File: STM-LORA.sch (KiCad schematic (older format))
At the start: 22 parts, among them J1 Batt, J10 CONN_02X07, J11 CONN_02X09, J12 CONN_01X02, J13 CONN_01X02, J14 CONN_01X02, J15 CONN_01X03, J2 Solar, J3 CONN_01X17, J4 CONN_01X03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

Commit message: edit front plane and readd fp-lib-table
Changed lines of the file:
@@
 LIBS:stm32f103c8t6-module-china
 LIBS:RFM95
+LIBS:STM-LORA-cache
 EELAYER 25 0
 EELAYER END
@@
 $EndComp
 Wire Wire Line
-	7750 1900 8800 1900
-Wire Wire Line
-	8800 1900 9100 1900
+	7750 1900 9100 1900
 Wire Wire Line
 	3900 3600 4700 3600
@@
 	6000 3400 6000 6500
 Wire Wire Line
-	6000 6500 1100 6500
-Wire Wire Line
-	1100 6500 1100 4050
-Wire Wire Line
-	1100 4050 1100 2050
+	1100 6500 6000 6500
+Wire Wire Line
+	1100 2050 1100 6500
 Wire Wire Line
 	1100 4050 1800 4050
@@
 	8800 1900 8800 2250
 Wire Wire Line
-	8800 2850 9000 2850
-Wire Wire Line
-	9000 2850 9100 2850
+	8800 2850 9100 2850
 Wire Wire Line
 	7550 4500 8850 4500
@@
 	1700 4950 1800 4950
 Wire Wire Line
-	3900 2550 4400 2550
-Wire Wire Line
-	4400 2550 4800 2550
-Wire Wire Line
-	4800 2550 5250 2550
+	3900 2550 5250 2550
 Wire Wire Line
 	5250 2550 5250 2950
@@
 	5750 2150 6200 2150
 Wire Wire Line
-	2950 6950 2950 7050
-Wire Wire Line
-	2950 7050 2950 7150
-Wire Wire Line
-	2950 7150 2950 7250
-Wire Wire Line
-	2950 7250 2950 7350
+	2950 6950 2950 7350
 Connection ~ 2950 7050
 Connection ~ 2950 7150
@@
 $EndComp
 Wire Wire Line
-	3500 6950 3500 7050
-Wire Wire Line
-	3500 7050 3500 7150
-Wire Wire Line
-	3500 7150 3500 7250
-Wire Wire Line
-	3500 7250 3500 7350
+	3500 6950 3500 7350
 Connection ~ 3500 7050
 Connection ~ 3500 7150

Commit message: Start bigger NG board
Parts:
- added J16: CONN_01X01, Pin_Headers:Pin_Header_Straight_1x01_Pitch2.54mm, symbol CONN_01X01
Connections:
- net at U2.9 (ANA): now also J16.1 (P1)
- no-connect marks 48 -> 47
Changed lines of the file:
@@
 Sheet 1 1
 Title "STM32 RFM95 Proto Board"
-Date "2017-04-01"
-Rev "0.2"
+Date "2017-06-10"
+Rev "0.3"
 Comp "http://v7f.eu"
 Comment1 ""
@@
 $EndComp
 NoConn ~ 3900 4800
-NoConn ~ 4700 3150
 NoConn ~ 5800 3500
 NoConn ~ 5800 3600
@@
 	6000 3400 6000 6500
 Wire Wire Line
-	1100 6500 6000 6500
-Wire Wire Line
-	1100 2050 1100 6500
+	6000 6500 1100 6500
+Wire Wire Line
+	1100 6500 1100 2050
 Wire Wire Line
 	1100 4050 1800 4050
@@
 NoConn ~ 9400 5650
 NoConn ~ 9400 5750
+$Comp
+L CONN_01X01 J16
+U 1 1 593BCF25
+P 4700 2950
+F 0 "J16" H 4700 3050 50  0000 C CNN
+F 1 "CONN_01X01" V 4800 2950 50  0000 C CNN
+F 2 "Pin_Headers:Pin_Header_Straight_1x01_Pitch2.54mm" H 4700 2950 50  0001 C CNN
+F 3 "" H 4700 2950 50  0001 C CNN
+	1    4700 2950
+	0    -1   -1   0
+$EndComp
 $EndSCHEMATC

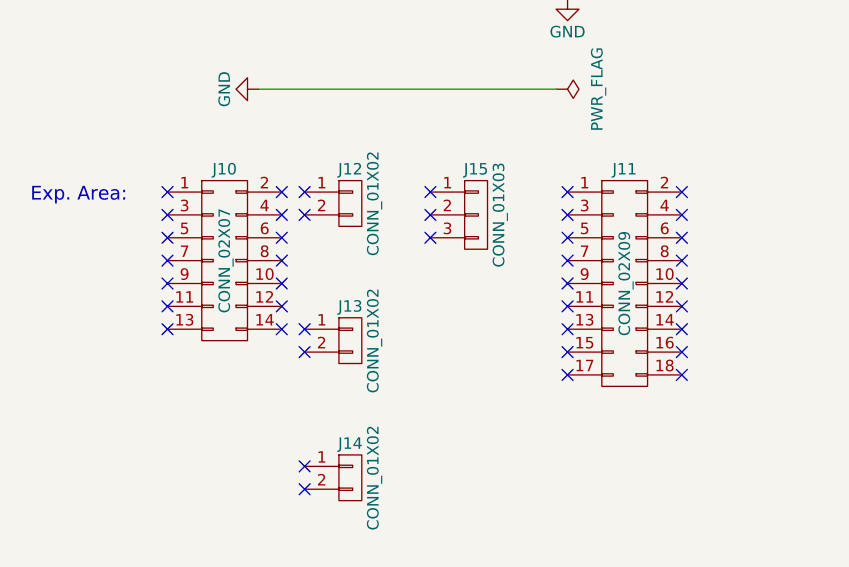
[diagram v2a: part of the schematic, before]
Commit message: Connect pads (breadboard like)
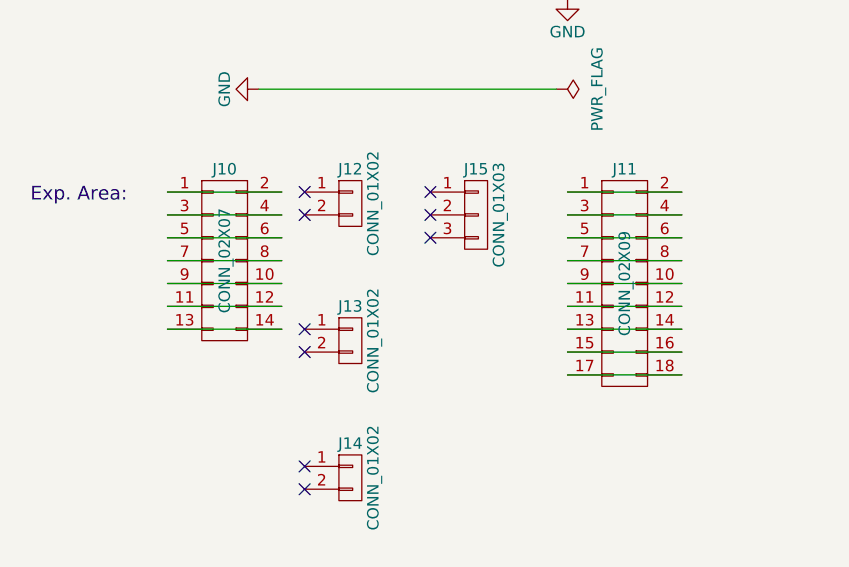
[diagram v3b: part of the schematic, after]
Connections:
- net at J10.1 (P1): now also J10.2 (P2)
- net at J10.10 (P10): now also J10.9 (P9)
- net at J10.11 (P11): now also J10.12 (P12)
- net at J10.13 (P13): now also J10.14 (P14)
- net at J10.3 (P3): now also J10.4 (P4)
- net at J10.5 (P5): now also J10.6 (P6)
- net at J10.7 (P7): now also J10.8 (P8)
- net at J11.1 (P1): now also J11.2 (P2)
- net at J11.10 (P10): now also J11.9 (P9)
- net at J11.11 (P11): now also J11.12 (P12)
- net at J11.13 (P13): now also J11.14 (P14)
- net at J11.15 (P15): now also J11.16 (P16)
- net at J11.17 (P17): now also J11.18 (P18)
- net at J11.3 (P3): now also J11.4 (P4)
- net at J11.5 (P5): now also J11.6 (P6)
- net at J11.7 (P7): now also J11.8 (P8)
- no-connect marks 47 -> 15
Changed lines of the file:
@@
 	1    0    0    -1
 $EndComp
-NoConn ~ 7150 4950
-NoConn ~ 7150 5050
-NoConn ~ 7150 5150
-NoConn ~ 7150 5250
-NoConn ~ 7150 5350
-NoConn ~ 7150 5450
-NoConn ~ 7150 5550
-NoConn ~ 7650 4950
-NoConn ~ 7650 5050
-NoConn ~ 7650 5150
-NoConn ~ 7650 5250
-NoConn ~ 7650 5350
-NoConn ~ 7650 5450
-NoConn ~ 7650 5550
 NoConn ~ 7750 4950
 NoConn ~ 7750 5050
@@
 NoConn ~ 8300 5050
 NoConn ~ 8300 5150
-NoConn ~ 8900 4950
-NoConn ~ 8900 5050
-NoConn ~ 8900 5150
-NoConn ~ 8900 5250
-NoConn ~ 8900 5350
-NoConn ~ 8900 5450
-NoConn ~ 8900 5550
-NoConn ~ 8900 5650
-NoConn ~ 8900 5750
-NoConn ~ 9400 4950
-NoConn ~ 9400 5050
-NoConn ~ 9400 5150
-NoConn ~ 9400 5250
-NoConn ~ 9400 5350
-NoConn ~ 9400 5450
-NoConn ~ 9400 5550
-NoConn ~ 9400 5650
-NoConn ~ 9400 5750
 $Comp
 L CONN_01X01 J16
@@
 	0    -1   -1   0
 $EndComp
+Wire Wire Line
+	8900 4950 9400 4950
+Wire Wire Line
+	8900 5050 9400 5050
+Wire Wire Line
+	9400 5150 8900 5150
+Wire Wire Line
+	8900 5250 9400 5250
+Wire Wire Line
+	9400 5350 8900 5350
+Wire Wire Line
+	8900 5450 9400 5450
+Wire Wire Line
+	9400 5550 8900 5550
+Wire Wire Line
+	8900 5650 9400 5650
+Wire Wire Line
+	8900 5750 9400 5750
+Wire Wire Line
+	7150 4950 7650 4950
+Wire Wire Line
+	7650 5050 7150 5050
+Wire Wire Line
+	7150 5150 7650 5150
+Wire Wire Line
+	7150 5250 7650 5250
+Wire Wire Line
+	7150 5350 7650 5350
+Wire Wire Line
+	7650 5450 7150 5450
+Wire Wire Line
+	7150 5550 7650 5550
 $EndSCHEMATC

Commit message: Convert libs for Kicad 5.1
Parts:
- C1: symbol CP -> STM-LORA-rescue:CP
- C2: symbol C -> STM-LORA-rescue:C
- D1: symbol D_Schottky -> STM-LORA-rescue:D_Schottky
- J1, J2: symbol CONN_01X02_MALE -> STM-LORA-rescue:CONN_01X02_MALE
- J10: symbol CONN_02X07 -> STM-LORA-rescue:CONN_02X07
- J11: symbol CONN_02X09 -> STM-LORA-rescue:CONN_02X09
- J12, J13, J14: symbol CONN_01X02 -> STM-LORA-rescue:CONN_01X02
- J15, J4, J5: symbol CONN_01X03 -> STM-LORA-rescue:CONN_01X03
- J16, J6: symbol CONN_01X01 -> STM-LORA-rescue:CONN_01X01
- J3: symbol CONN_01X17 -> STM-LORA-rescue:CONN_01X17
- J7: symbol CONN_01X14 -> STM-LORA-rescue:CONN_01X14
- J8, J9: symbol CONN_01X05 -> STM-LORA-rescue:CONN_01X05
- R1, R2: symbol R -> STM-LORA-rescue:R
- U1: symbol stm32f103c8t6-module-china -> stm32f103c8t6-module-china:stm32f103c8t6-module-china
- U2: symbol RFM95HW -> RFM95:RFM95HW
